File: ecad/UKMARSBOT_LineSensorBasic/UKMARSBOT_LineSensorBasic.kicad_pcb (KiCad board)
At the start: 2 copper layers, 40.8 x 81.4 mm, 32 parts, among them J1 Conn_01x16, Q1 BC337, Q2 BPW85C, Q3 BPW85C, Q4 BPW85C, Q5 BPW85C, Q6 BC337

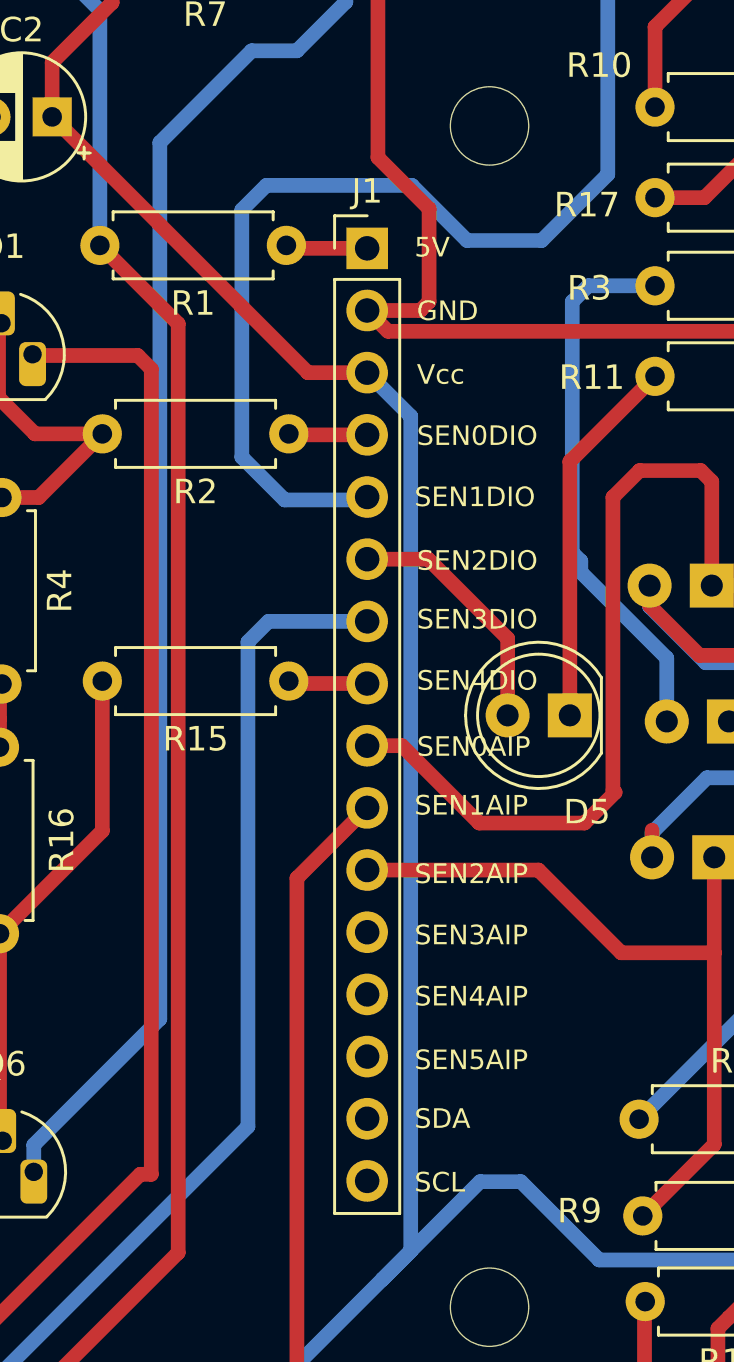
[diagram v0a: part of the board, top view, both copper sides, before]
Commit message: Connectors moved to be on common 0.1" Grid and wheel cutouts included
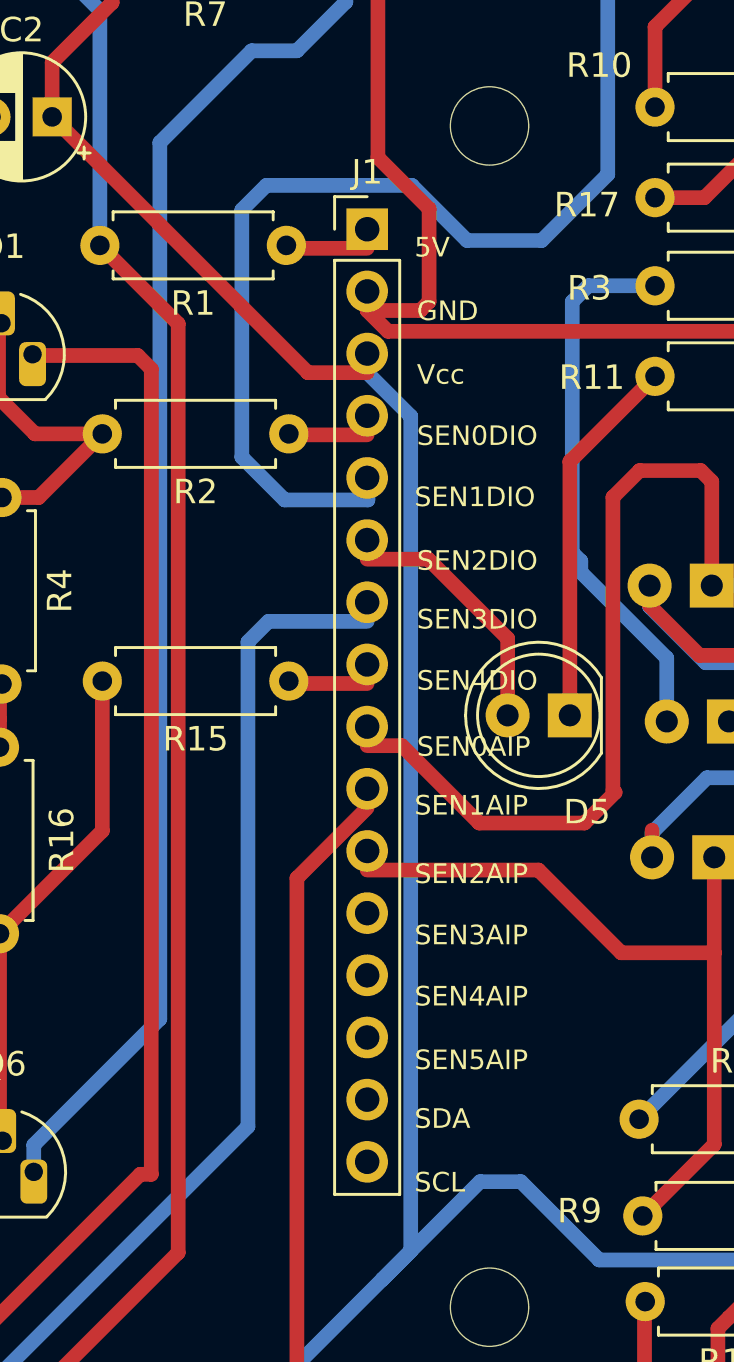
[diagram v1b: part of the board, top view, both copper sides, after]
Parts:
- moved J1 0.78 mm to (139.4, 85.1)
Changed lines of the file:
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@@
 		(locked yes)
 		(layer "F.Cu")
-		(at 139.37 85.87)
+		(at 139.37 85.09)
 		(descr "Through hole straight pin header, 1x16, 2.54mm pitch, single row")
 		(tags "Through hole pin header THT 1x16 2.54mm single row")
@@
 		(min_thickness 0.25)
 		(filled_areas_thickness no)
-		(fill yes
+		(fill
 			(thermal_gap 0.5)
 			(thermal_bridge_width 0.5)

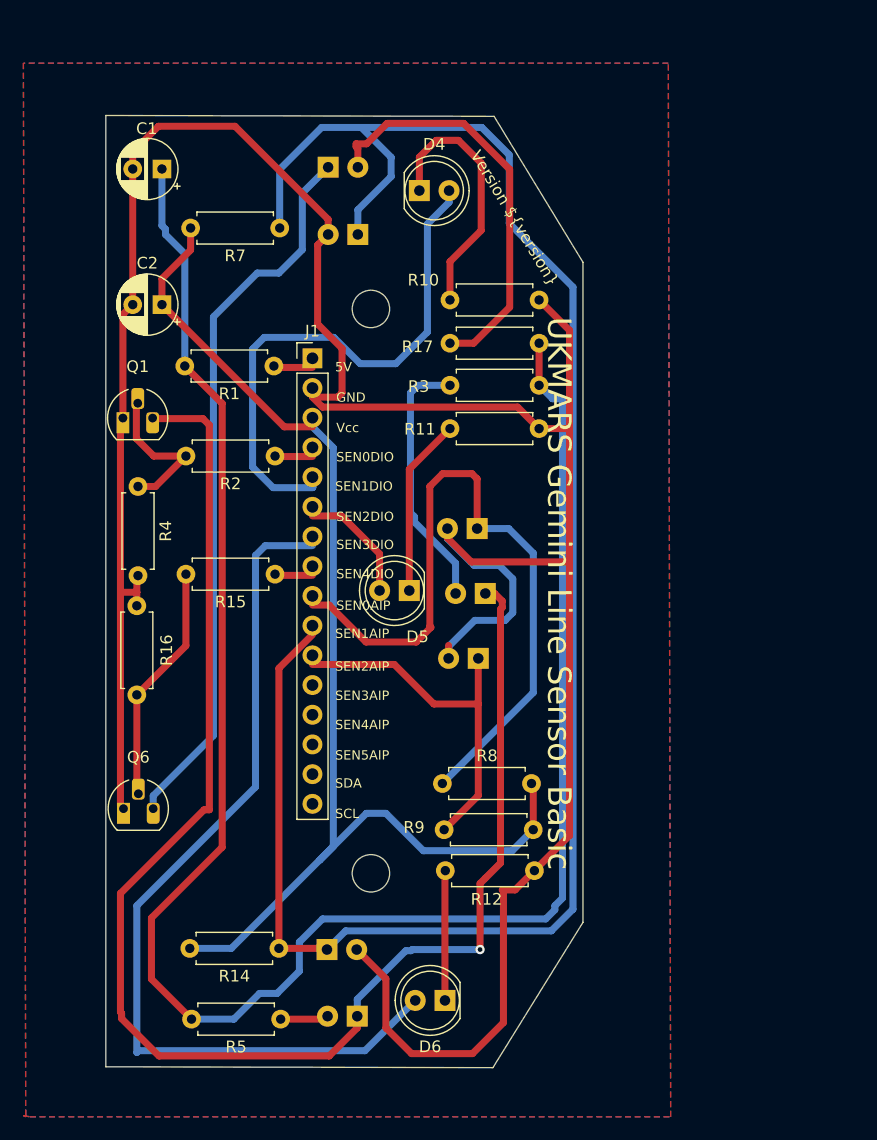
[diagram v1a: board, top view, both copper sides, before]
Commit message: Basic line sensor modified for new connector position
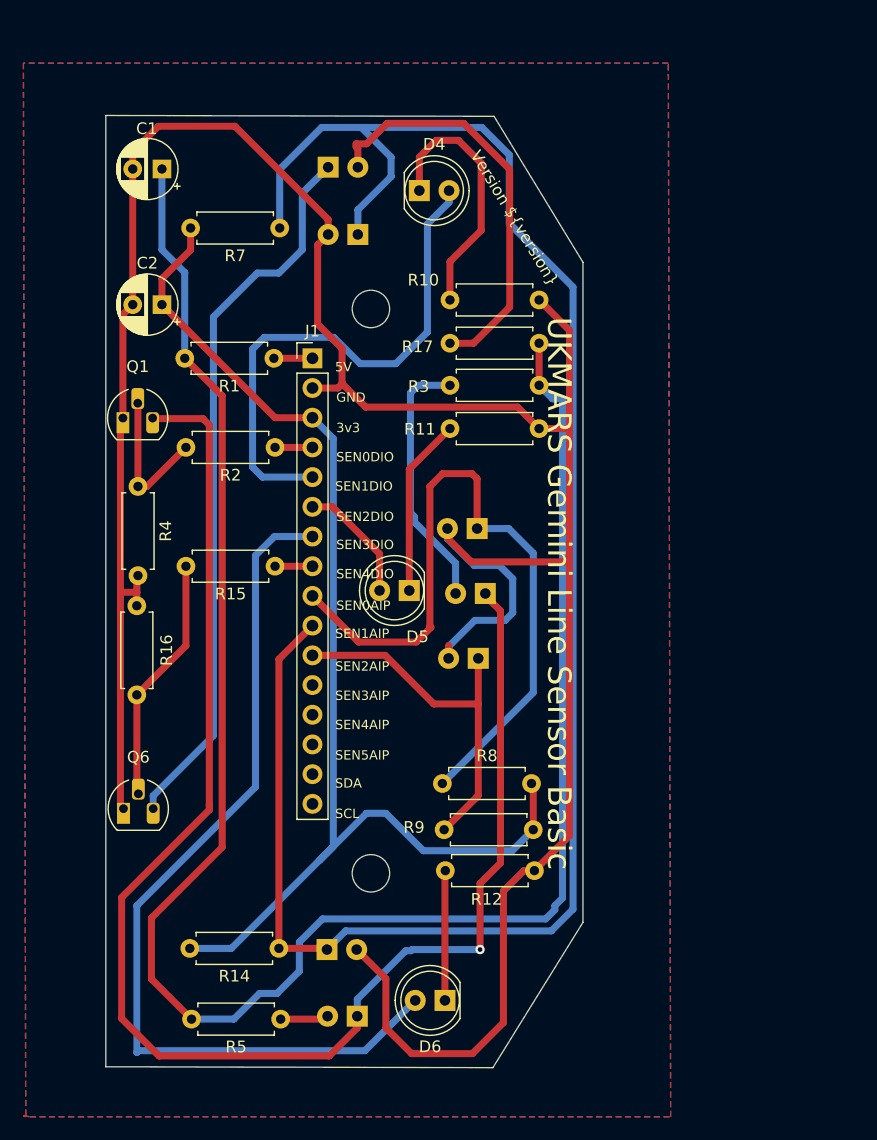
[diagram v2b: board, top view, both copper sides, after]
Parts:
- moved R2 0.74 mm to (136.2, 92.7)
- moved R15 0.68 mm to (136.2, 102.9)
- moved R1 0.66 mm to (136.1, 85.1)
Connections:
- net Vcc renamed 3v3
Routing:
- net GND: track 241.0 -> 238.0 mm
- net SEN1AIP: track 159.9 -> 160.7 mm
- net Net-(Q6-B): track 20.6 -> 21.3 mm
- net Net-(D1-K): track 129.0 -> 128.3 mm
- net SEN1DI0: track 46.4 -> 45.9 mm
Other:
- board text added: "3v3"
- board text removed: "Vcc"

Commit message: Revised lime sensor board and sensor mounting hole moved forward 1.27mm for connector
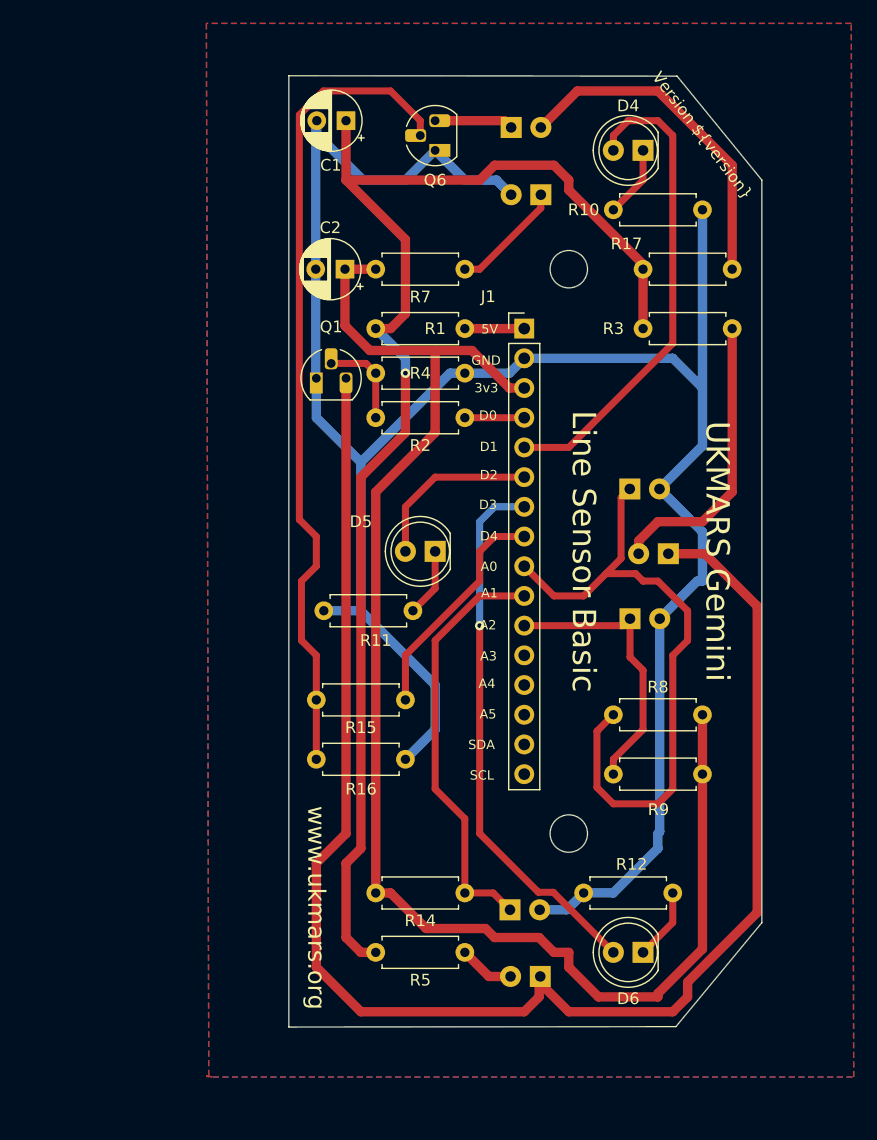
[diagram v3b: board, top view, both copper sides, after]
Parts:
- R10, R11, R12: value 330R -> 680R
- moved Q6 62.3 mm to (149.9, 67.3), turned to 90 degrees
- moved R17 24.9 mm to (175.3, 77.5), turned to 180 degrees
- moved R3 24.6 mm to (175.3, 82.5), turned to 180 degrees
- moved R4 22.5 mm to (144.8, 86.4), turned to 0 degrees
- moved R12 19.5 mm to (170.2, 130.8), turned to 180 degrees
- moved D4 19.4 mm to (167.6, 67.3), turned to 180 degrees
- moved J1 18.3 mm to (157.5, 82.5)
- moved D6 17.4 mm to (167.6, 135.9)
- moved H3 17.3 mm to (161.3, 77.5)
- moved H4 17.3 mm to (161.3, 125.7)
- moved Q1 16.9 mm to (139.7, 86.8)
- moved R5 16.8 mm to (152.4, 135.9)
- moved R14 16.6 mm to (152.4, 130.8)
- moved R1 16.5 mm to (152.4, 82.5)
- moved R2 16.4 mm to (152.4, 90.2)
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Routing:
- net SEN1AIP: track 160.7 -> 46.1 mm
- net Net-(D7-K): track 62.1 -> 6.74 mm
- net Vemit: track 165.2 -> 115.4 mm, vias 0 -> 1
- net Net-(Q6-B): track 21.3 -> 70.3 mm
- net GND: track 238.0 -> 190.8 mm
- net SEN3DI0: track 77.9 -> 46.6 mm, vias 0 -> 1
- net 3v3: track 103.7 -> 127.8 mm
- net SEN4DI0: track 3.20 -> 19.7 mm
- net Net-(D4-K): track 22.4 -> 6.13 mm
- net Net-(D5-K): track 15.3 -> 5.86 mm
- net SEN2AIP: track 31.8 -> 24.1 mm
- net Net-(D7-A): track 35.7 -> 29.2 mm
- net SEN0AIP: track 61.9 -> 55.4 mm
- net Net-(D1-K): track 128.3 -> 134.4 mm, vias 1 -> 0
- net Net-(D6-K): track 11.1 -> 6.13 mm
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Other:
- board size 40.8 x 81.4 mm -> 40.5 x 81.4 mm
- board text added: "A0"
- board text added: "A1"
- board text added: "A2"
- board text added: "A3"
- board text added: "A4"
- board text added: "A5"
- board text added: "D0"
- board text added: "D1"
- board text added: "D2"
- board text added: "D3"
- board text added: "D4"
- board text added: "Line Sensor Basic"
- board text added: "UKMARS Gemini"
- board text added: "Version 1.0"
- board text added: "www.ukmars.org"
- board text removed: "SEN0AIP"
- board text removed: "SEN0DIO"
- board text removed: "SEN1AIP"
- board text removed: "SEN1DIO"
- board text removed: "SEN2AIP"
- board text removed: "SEN2DIO"
- board text removed: "SEN3AIP"
- board text removed: "SEN3DIO"
- board text removed: "SEN4AIP"
- board text removed: "SEN4DIO"
- board text removed: "SEN5AIP"

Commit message: Revised Wall Sensor Board consistent with hole and connector position. Fabrication files created.
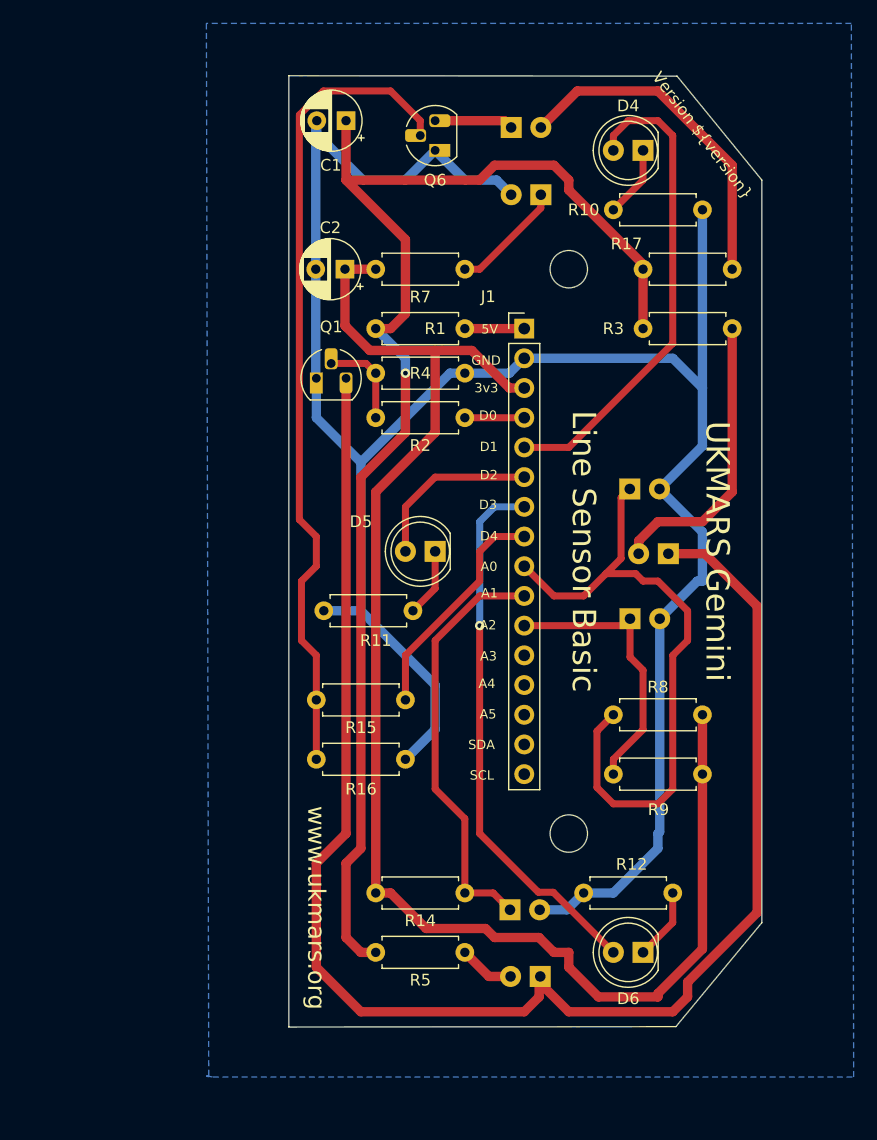
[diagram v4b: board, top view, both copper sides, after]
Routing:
- removed copper zone on F.Cu, net GND
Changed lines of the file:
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@@
 			(outputformat 1)
 			(mirror no)
-			(drillshape 1)
+			(drillshape 0)
 			(scaleselection 1)
-			(outputdirectory "")
+			(outputdirectory "fab/")
 		)
 	)
@@
 		(tags "Resistor Axial_DIN0207 series Axial Horizontal pin pitch 7.62mm 0.25W = 1/4W length 6.3mm diameter 2.5mm")
 		(property "Reference" "R12"
-			(at 3.52 2.45 360)
+			(at 3.52 2.45 0)
 			(layer "F.SilkS")
 			(effects
@@
 		)
 		(property "Value" "680R"
-			(at 3.81 2.37 360)
+			(at 3.81 2.37 0)
 			(layer "F.Fab")
 			(effects
@@
 		)
 		(fp_text user "${REFERENCE}"
-			(at 3.81 0 360)
+			(at 3.81 0 0)
 			(layer "F.Fab")
 			(effects
@@
 		(tags "Resistor Axial_DIN0207 series Axial Horizontal pin pitch 7.62mm 0.25W = 1/4W length 6.3mm diameter 2.5mm")
 		(property "Reference" "R3"
-			(at 10.16 0 360)
+			(at 10.16 0 0)
 			(layer "F.SilkS")
 			(effects
@@
 		)
 		(property "Value" "10R"
-			(at 3.81 2.37 360)
+			(at 3.81 2.37 0)
 			(layer "F.Fab")
 			(effects
@@
 		)
 		(fp_text user "${REFERENCE}"
-			(at 3.81 0 360)
+			(at 3.81 0 0)
 			(layer "F.Fab")
 			(effects
@@
 		(tags "Resistor Axial_DIN0207 series Axial Horizontal pin pitch 7.62mm 0.25W = 1/4W length 6.3mm diameter 2.5mm")
 		(property "Reference" "R17"
-			(at 9.043665 2.166793 360)
+			(at 9.043665 2.166793 0)
 			(layer "F.SilkS")
 			(effects
@@
 		)
 		(property "Value" "10R"
-			(at 3.81 2.37 360)
+			(at 3.81 2.37 0)
 			(layer "F.Fab")
 			(effects
@@
 		)
 		(fp_text user "${REFERENCE}"
-			(at 3.81 0 360)
+			(at 3.81 0 0)
 			(layer "F.Fab")
 			(effects
@@
 		(tags "Resistor Axial_DIN0207 series Axial Horizontal pin pitch 7.62mm 0.25W = 1/4W length 6.3mm diameter 2.5mm")
 		(property "Reference" "R11"
-			(at 3.180737 -2.544173 360)
+			(at 3.180737 -2.544173 0)
 			(layer "F.SilkS")
 			(effects
@@
 		)
 		(property "Value" "680R"
-			(at 3.81 2.37 360)
+			(at 3.81 2.37 0)
 			(layer "F.Fab")
 			(effects
@@
 		)
 		(fp_text user "${REFERENCE}"
-			(at 3.81 0 360)
+			(at 3.81 0 0)
 			(layer "F.Fab")
 			(effects
@@
 		(tags "Resistor Axial_DIN0207 series Axial Horizontal pin pitch 7.62mm 0.25W = 1/4W length 6.3mm diameter 2.5mm")
 		(property "Reference" "R16"
-			(at 3.82 2.55 360)
+			(at 3.82 2.55 0)
 			(layer "F.SilkS")
 			(effects
@@
 		)
 		(property "Value" "10K"
-			(at 3.81 2.37 360)
+			(at 3.81 2.37 0)
 			(layer "F.Fab")
 			(effects
@@
 		)
 		(fp_text user "${REFERENCE}"
-			(at 3.81 0 360)
+			(at 3.81 0 0)
 			(layer "F.Fab")
 			(effects
@@
 		)
 		(property "Value" "10K"
-			(at 3.81 2.37 360)
+			(at 3.81 2.37 0)
 			(layer "F.Fab")
 			(effects
@@
 		)
 		(fp_text user "${REFERENCE}"
-			(at 3.81 0 360)
+			(at 3.81 0 0)
 			(layer "F.Fab")
 			(effects
@@
 		(tags "LED")
 		(property "Reference" "D4"
-			(at 1.27 3.81 360)
+			(at 1.27 3.81 0)
 			(layer "F.SilkS")
 			(effects
@@
 		)
 		(property "Value" "Radius"
-			(at 1.27 3.96 360)
+			(at 1.27 3.96 0)
 			(layer "F.Fab")
 			(effects
@@
 		)
 		(property "Footprint" "LED_THT:LED_D5.0mm"
-			(at 0 0 360)
+			(at 0 0 0)
 			(layer "F.Fab")
 			(hide yes)
@@
 		)
 		(property "Datasheet" ""
-			(at 0 0 360)
+			(at 0 0 0)
 			(layer "F.Fab")
 			(hide yes)
@@
 		)
 		(property "Description" ""
-			(at 0 0 360)
+			(at 0 0 0)
 			(layer "F.Fab")
 			(hide yes)
@@
 		)
 		(fp_text user "${REFERENCE}"
-			(at 1.27 0 360)
+			(at 1.27 0 0)
 			(layer "F.Fab")
 			(effects
@@
 		(tags "LED")
 		(property "Reference" "Q4"
-			(at -2.5 0.05 360)
+			(at -2.5 0.05 0)
 			(layer "B.SilkS")
 			(effects
@@
 		)
 		(property "Value" "BPW85C"
-			(at 1.27 -2.96 360)
+			(at 1.27 -2.96 0)
 			(layer "B.Fab")
 			(effects
@@
 		)
 		(property "Footprint" "LED_THT:LED_D3.0mm_Clear"
-			(at 0 0 360)
+			(at 0 0 0)
 			(layer "B.Fab")
 			(hide yes)
@@
 		)
 		(property "Datasheet" "https://www.vishay.com/docs/81531/bpw85a.pdf"
-			(at 0 0 360)
+			(at 0 0 0)
 			(layer "B.Fab")
 			(hide yes)
@@
 		)
 		(property "Description" ""
-			(at 0 0 360)
+			(at 0 0 0)
 			(layer "B.Fab")
 			(hide yes)
@@
 		)
 		(fp_text user "${REFERENCE}"
-			(at 1.27 0 360)
+			(at 1.27 0 0)
 			(layer "B.Fab")
 			(effects
@@
 		(tags "LED")
 		(property "Reference" "Q3"
-			(at -2.7 -0.05 360)
+			(at -2.7 -0.05 0)
 			(layer "B.SilkS")
 			(effects
@@
 		)
 		(property "Value" "BPW85C"
-			(at 1.27 -2.96 360)
+			(at 1.27 -2.96 0)
 			(layer "B.Fab")
 			(effects
@@
 		)
 		(property "Footprint" "LED_THT:LED_D3.0mm_Clear"
-			(at 0 0 360)
+			(at 0 0 0)
 			(layer "B.Fab")
 			(hide yes)
@@
 		)
 		(property "Datasheet" "https://www.vishay.com/docs/81531/bpw85a.pdf"
-			(at 0 0 360)
+			(at 0 0 0)
 			(layer "B.Fab")
 			(hide yes)
@@
 		)
 		(property "Description" ""
-			(at 0 0 360)
+			(at 0 0 0)
 			(layer "B.Fab")
 			(hide yes)
@@
 		)
 		(fp_text user "${REFERENCE}"
-			(at 1.27 0 360)
+			(at 1.27 0 0)
 			(layer "B.Fab")
 			(effects
@@
 		(net 1)
 		(net_name "GND")
-		(layers "F&B.Cu")
+		(layer "B.Cu")
 		(hatch edge 0.5)
 		(connect_pads
